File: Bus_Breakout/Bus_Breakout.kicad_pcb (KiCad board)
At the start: 2 copper layers, 223.5 x 104.6 mm, 44 parts, among them J1 AudioJack2_SwitchT, J10 AudioJack2_SwitchT, J11 AudioJack2_SwitchT, J12 AudioJack2_SwitchT, J13 AudioJack2_SwitchT, J14 AudioJack2_SwitchT, J15 AudioJack2_SwitchT, J16 AudioJack2_SwitchT, J17 AudioJack2_SwitchT, J18 AudioJack2_SwitchT, J19 AudioJack2_SwitchT, J2 AudioJack2_SwitchT, J20 AudioJack2_SwitchT, J21 AudioJack2_SwitchT, J22 AudioJack2_SwitchT, J23 AudioJack2_SwitchT, J24 AudioJack2_SwitchT, J25 AudioJack2_SwitchT, J26 AudioJack2_SwitchT, J27 AudioJack2_SwitchT, J28 AudioJack2_SwitchT, J29 AudioJack2_SwitchT, J3 AudioJack2_SwitchT, J30 AudioJack2_SwitchT, J31 AudioJack2_SwitchT, J32 AudioJack2_SwitchT, J33 AudioJack2_SwitchT, J34 AudioJack2_SwitchT, J35 AudioJack2_SwitchT, J36 AudioJack2_SwitchT, J37 AudioJack2_SwitchT, J38 AudioJack2_SwitchT, J39 AudioJack2_SwitchT, J4 AudioJack2_SwitchT, J40 AudioJack2_SwitchT, J41 Conn_02x20_Female, J42 Conn_02x20_Male, J43 Conn_02x20_Female, J44 Conn_02x20_Female, J5 AudioJack2_SwitchT, J6 AudioJack2_SwitchT, J7 AudioJack2_SwitchT, J8 AudioJack2_SwitchT, J9 AudioJack2_SwitchT

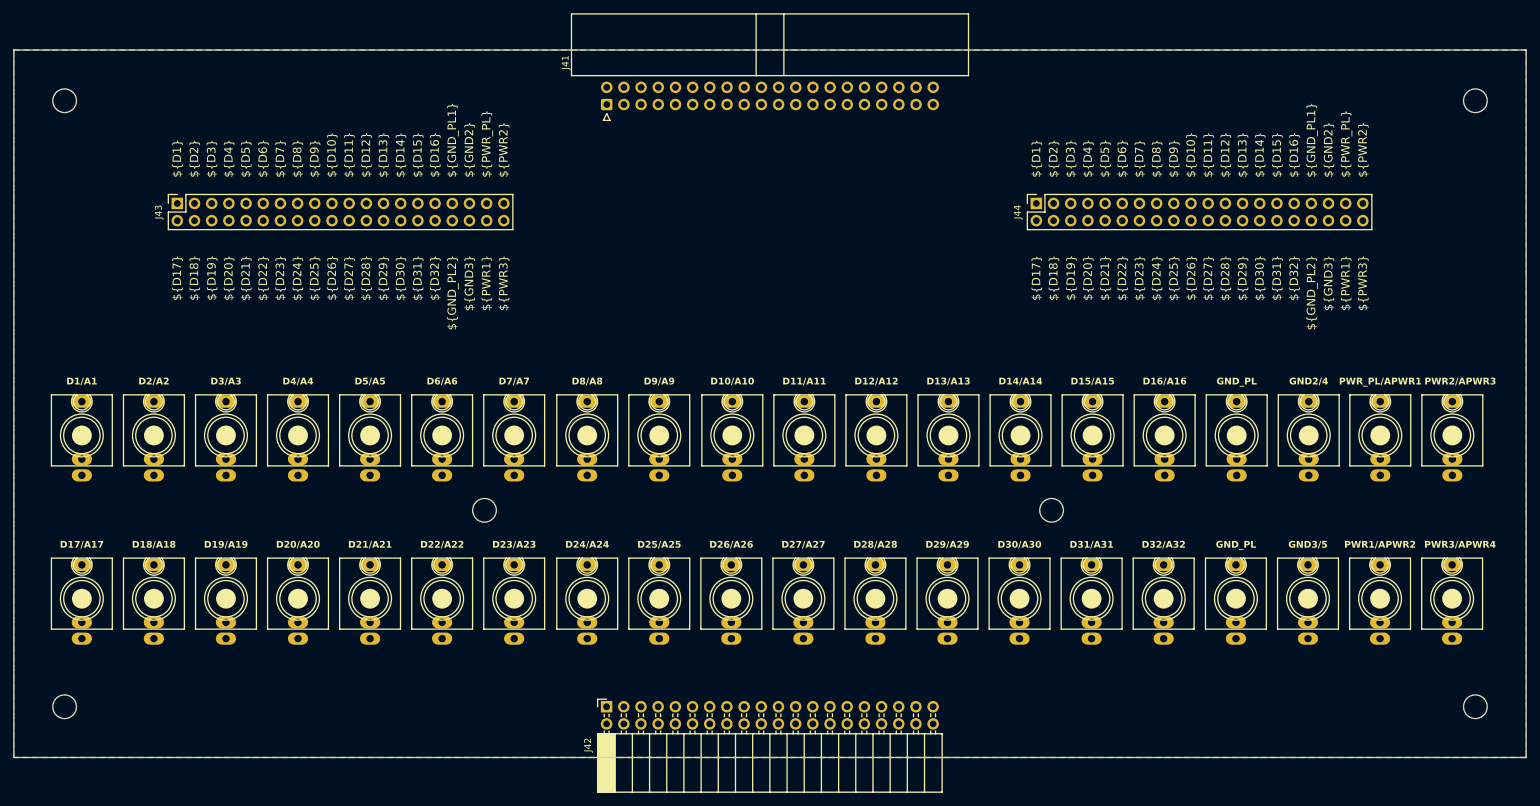
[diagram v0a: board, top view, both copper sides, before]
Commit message: Board Routed and Passing DRC. Still need some cleanup
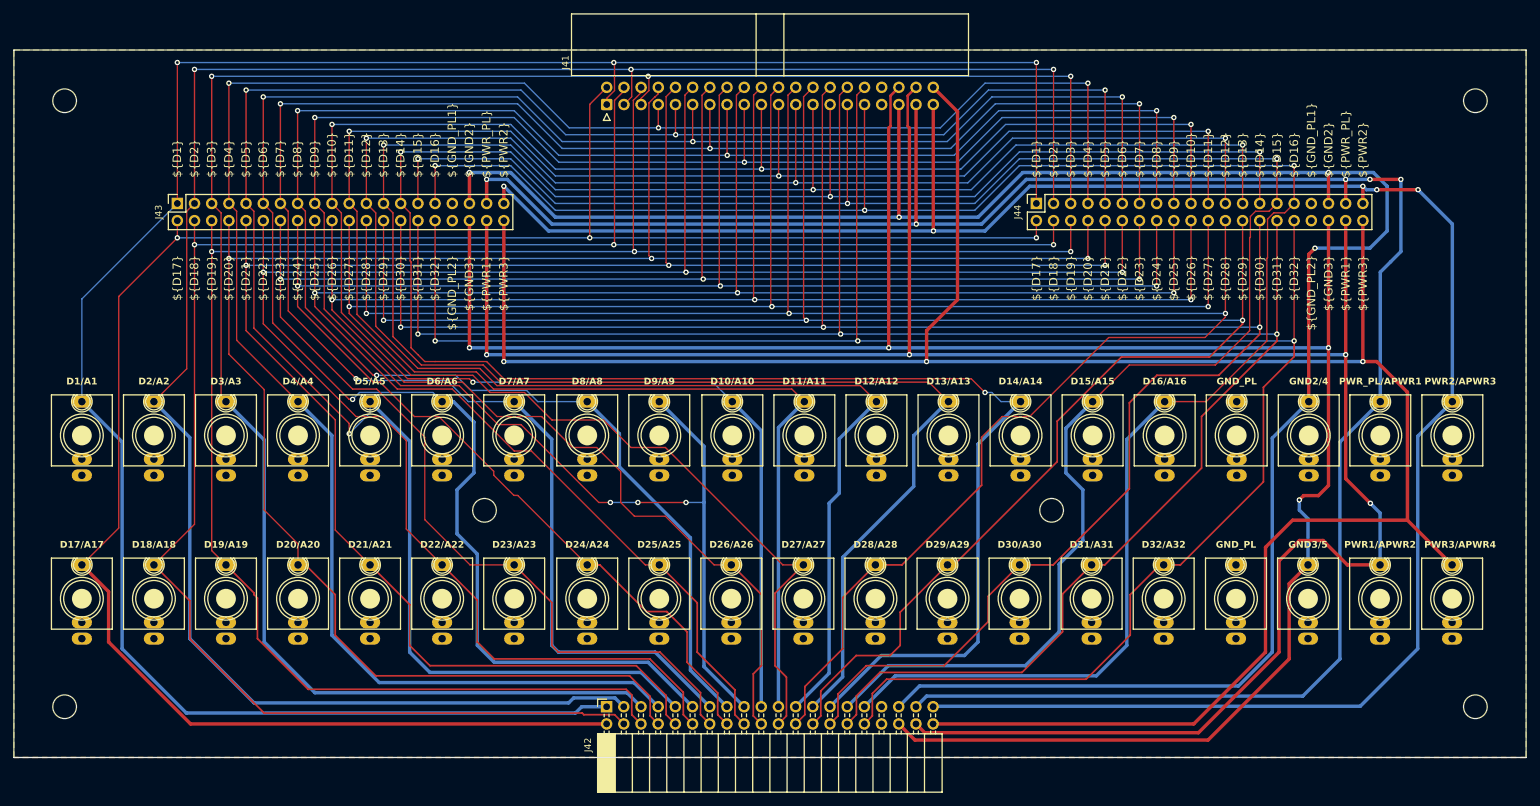
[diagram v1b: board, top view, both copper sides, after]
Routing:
- net PWR3/APWR4: track 0.00 -> 340.9 mm, vias 0 -> 3
- net D14/A14: track 0.00 -> 340.6 mm, vias 0 -> 4
- net PWR1/APWR2: track 0.00 -> 330.2 mm, vias 0 -> 4
- net D1/A1: track 0.00 -> 325.4 mm, vias 0 -> 3
- net D13/A13: track 0.00 -> 322.1 mm, vias 0 -> 3
- net GND3/5: track 0.00 -> 318.1 mm, vias 0 -> 4
- net PWR2/APWR3: track 0.00 -> 311.8 mm, vias 0 -> 5
- net D12/A12: track 0.00 -> 310.7 mm, vias 0 -> 3
- net D2/A2: track 0.00 -> 310.2 mm, vias 0 -> 3
- net GND2/4: track 0.00 -> 307.0 mm, vias 0 -> 4
- net PWR_PL/APWR1: track 0.00 -> 305.6 mm, vias 0 -> 5
- net D32/A32: track 0.00 -> 302.5 mm, vias 0 -> 3
- net D17/A17: track 0.00 -> 301.2 mm, vias 0 -> 3
- net D9/A9: track 0.00 -> 300.8 mm, vias 0 -> 6
- net D11/A11: track 0.00 -> 299.4 mm, vias 0 -> 3
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
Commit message: Board Routed and Passing DRC.Should be about ready to order
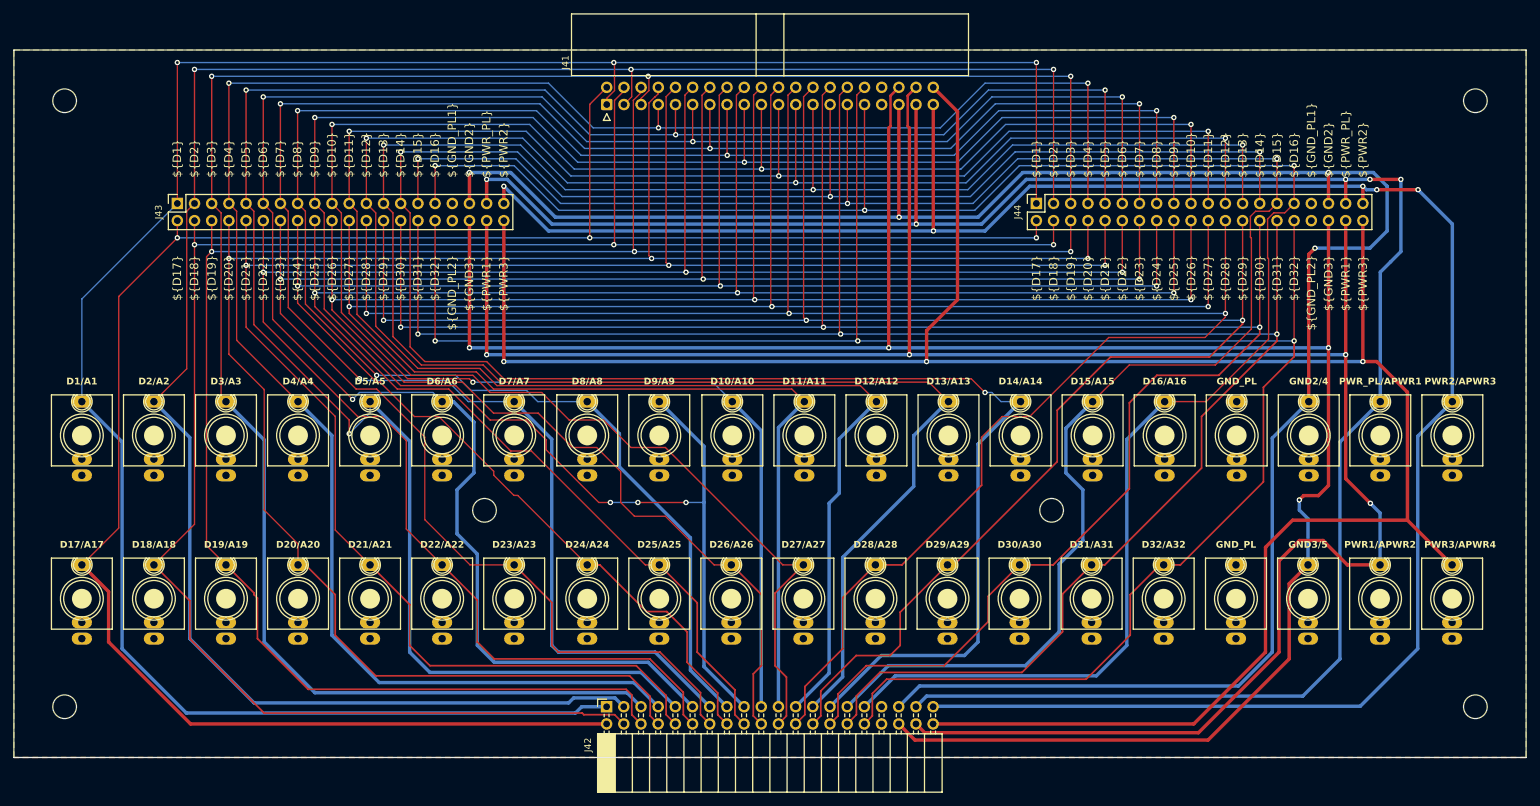
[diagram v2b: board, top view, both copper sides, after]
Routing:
- net D29/A29: track 288.7 -> 289.6 mm
- net D9/A9: track 300.8 -> 301.7 mm
- net D19/A19: track 284.6 -> 285.2 mm
